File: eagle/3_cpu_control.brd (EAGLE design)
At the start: 160 x 100 mm, 50 parts, among them IC1 74LS151N, IC10 74LS173N, IC11 74LS74N, IC12 74LS74N, IC13 74LS541N, IC14 74LS541N, IC15 74LS21N, IC16 74LS02N, IC17 74LS02N, IC18 74LS04N, IC2 74LS151N, IC20 74LS08N, IC3 74LS153N, IC4 74LS153N, IC5 74LS541N, IC6 74LS32N, IC7 74LS08N, IC8 74LS151N, IC9 74LS157N

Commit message: Renamed F6 to /FP
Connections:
- net F6 renamed /FP
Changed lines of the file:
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@@
 <wire x1="48.26" y1="57.4675" x2="48.26" y2="58.7375" width="0.4064" layer="1"/>
 </signal>
-<signal name="F6">
+<signal name="/FP">
 <contactref element="IC11" pad="9"/>
 <contactref element="IC5" pad="8"/>

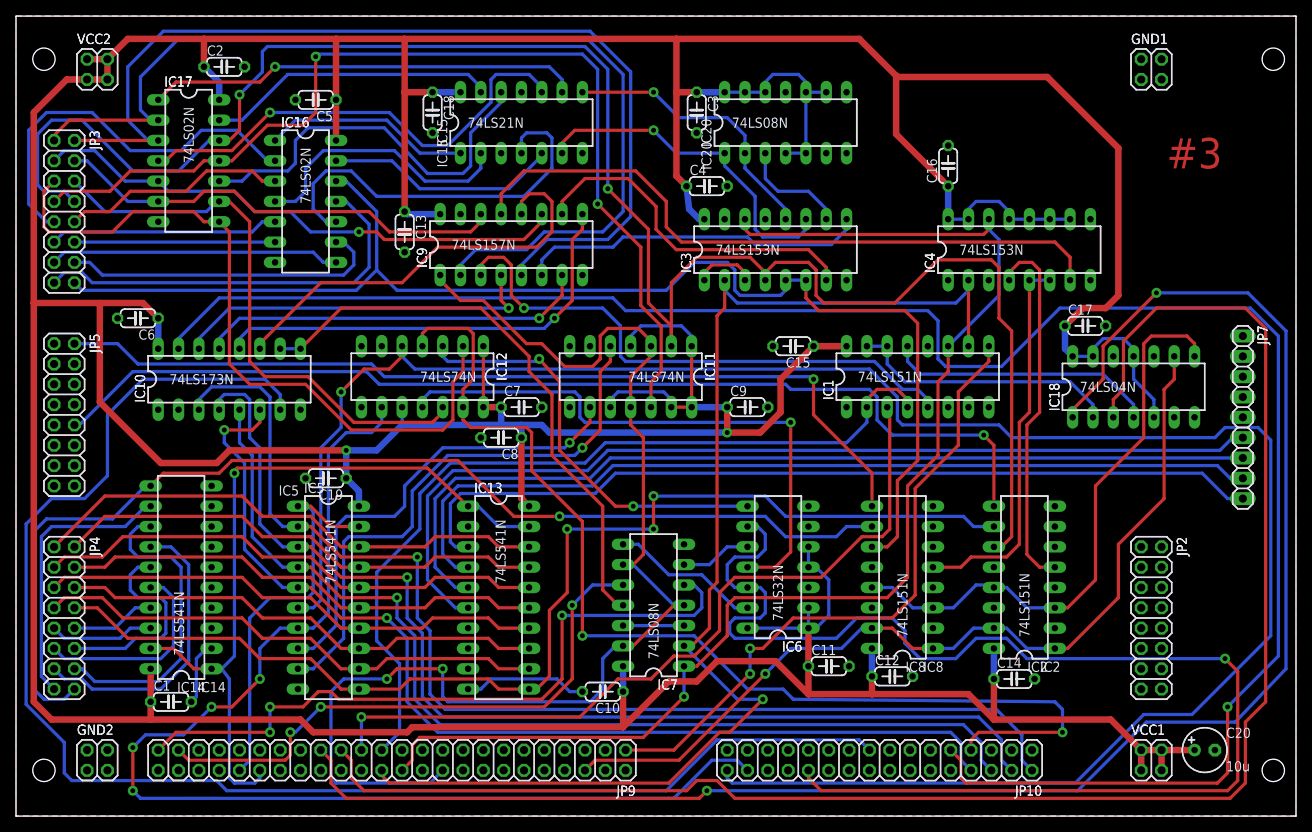
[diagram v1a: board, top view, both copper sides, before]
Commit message: Added /FP (flag paging enabled) to schematics and board, extended header connector
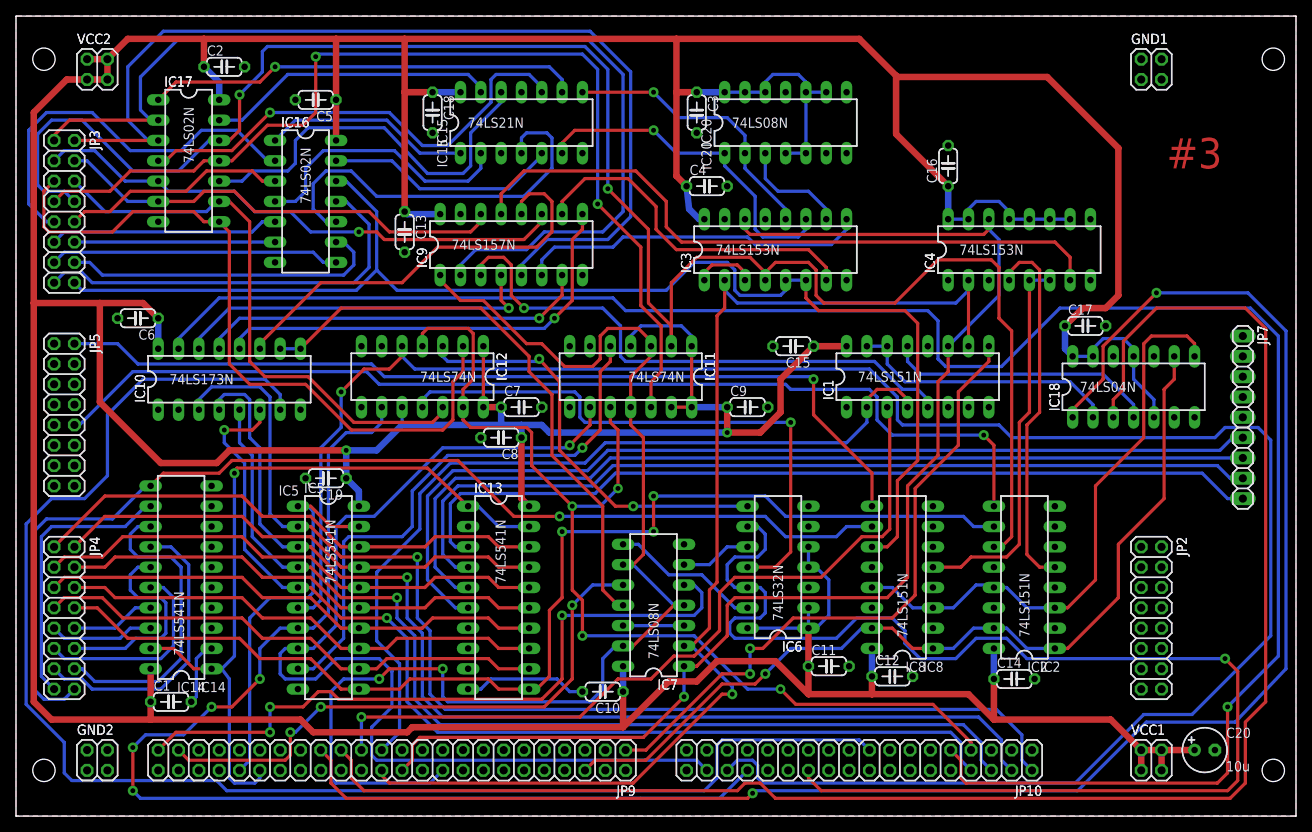
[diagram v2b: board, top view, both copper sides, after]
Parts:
- JP10: device pinhead:2X16 -> pinhead:2X18
- moved JP10 2.54 mm to (105.4, 6.99)
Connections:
- net +5V: no longer IC11.10
- net /FP: now also JP10.34
- net /RST: now also IC11.10
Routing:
- net /FP: track 58.9 -> 132.8 mm
- net +5V: track 853.1 -> 842.8 mm
- net /RST: track 136.7 -> 129.3 mm, vias 2 -> 4
- net LOAD_FLAGS1: track 156.6 -> 149.5 mm
- net CLK0D: track 184.2 -> 186.6 mm
- net /FI: track 259.2 -> 260.7 mm
- net /FS: track 149.1 -> 148.1 mm

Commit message: All boards prepared for MMU extension
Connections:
- new net /IO: JP10.35
- new net /NP_FAULT: JP10.36
- new net /WR_FAULT: JP10.33
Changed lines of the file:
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@@
 <contactref element="JP5" pad="4"/>
+</signal>
+<signal name="/WR_FAULT">
+<contactref element="JP10" pad="33"/>
+</signal>
+<signal name="/NP_FAULT">
+<contactref element="JP10" pad="36"/>
+</signal>
+<signal name="/IO">
+<contactref element="JP10" pad="35"/>
 </signal>
 </signals>

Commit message: Removal of PPC started
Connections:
- removed net /LDPPC: JP10.11
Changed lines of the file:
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@@
 <contactref element="JP10" pad="1"/>
-</signal>
-<signal name="/LDPPC">
-<contactref element="JP10" pad="11"/>
 </signal>
 <signal name="BUSCLKA">

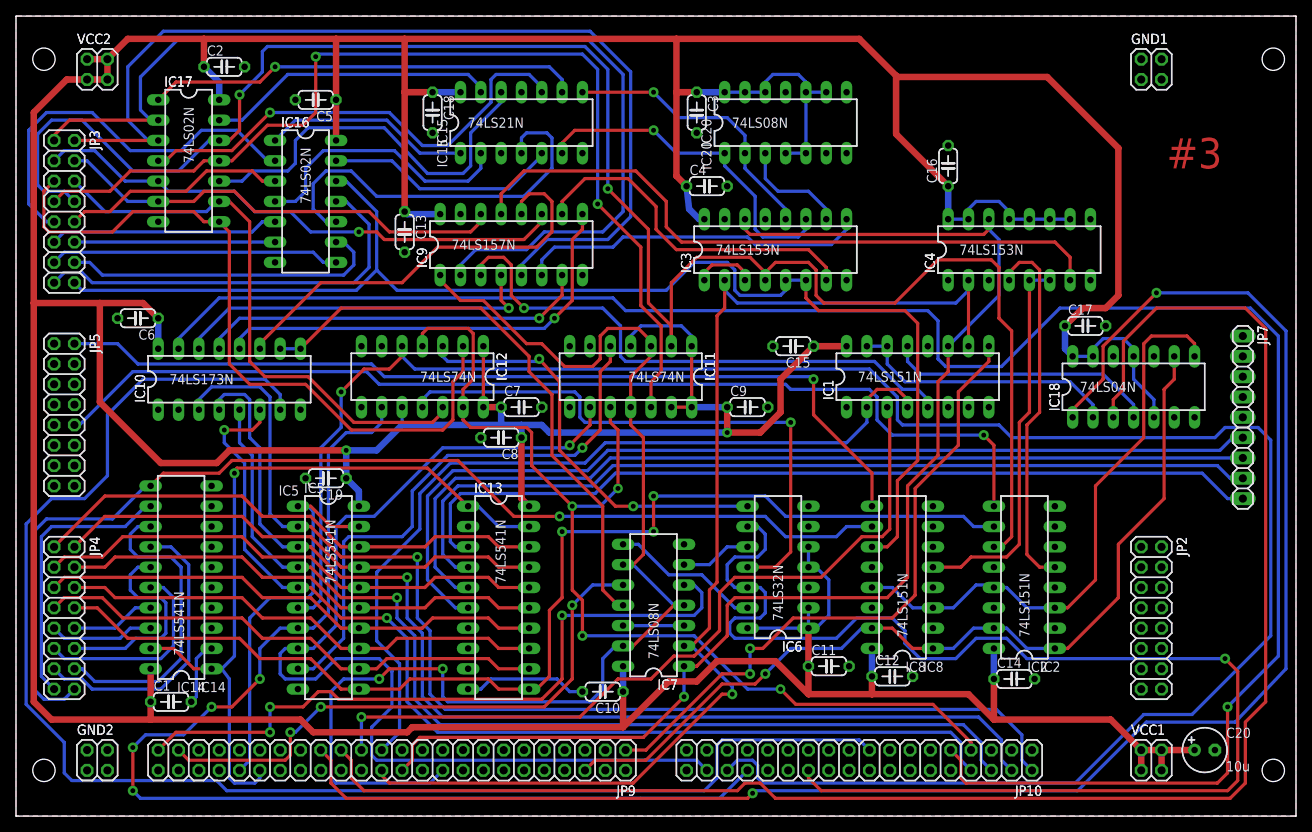
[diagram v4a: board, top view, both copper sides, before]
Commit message: Renumbered boards and schematic sheets
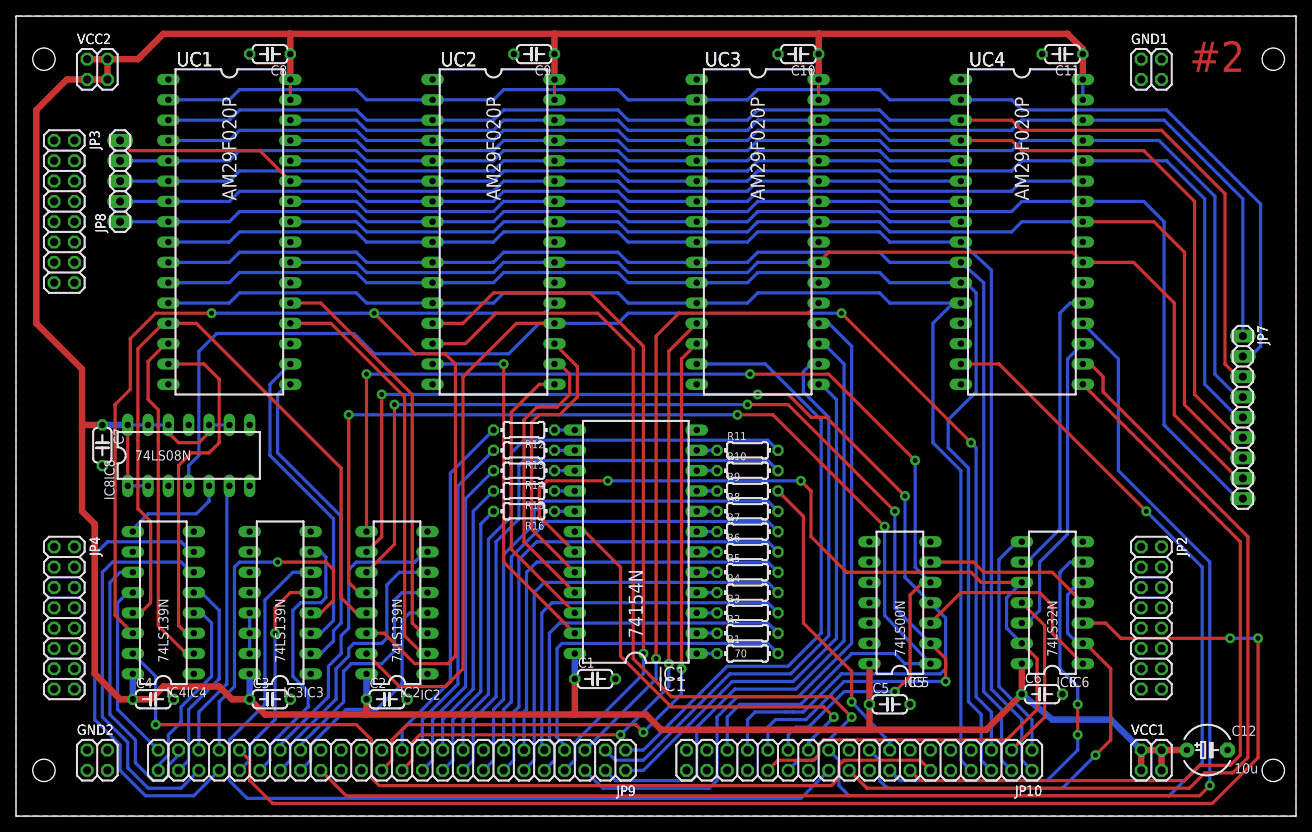
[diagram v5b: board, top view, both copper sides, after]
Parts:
- removed C13, C14, C15, C16, C17, C18, C19: 100n, rcl:C050-024X044
- removed C20: 10u, rcl:E2,5-6
- removed IC10: 74LS173N, 74xx-eu:DIL16
- removed IC11, IC12: 74LS74N, 74xx-eu:DIL14
- removed IC13, IC14: 74LS541N, 74xx-us:DIL20
- removed IC15: 74LS21N, 74xx-eu:DIL14
- removed IC16, IC17: 74LS02N, 74xx-eu:DIL14
- removed IC18: 74LS04N, 74xx-eu:DIL14
- removed IC20, IC7: 74LS08N, 74xx-eu:DIL14
- removed IC9: 74LS157N, 74xx-eu:DIL16
- removed JP5: (no value), pinhead:2X08
- added JP8: (no value), pinhead:1X05
- added R1: 70, rcl:0204/7
- added R10, R11, R12, R13, R14, R15, R16, R2, R3, R4, R5, R6, R7, R8, R9: (no value), rcl:0204/7
- added UC1, UC2, UC3, UC4: AM29F020P, am29-memory:DIL32-6
- C12: value 100n -> 10u; device rcl:C050-024X044 -> rcl:E5-6
- IC1: value 74LS151N -> 74154N; device 74xx-eu:DIL16 -> 74xx-eu:DIL24-6
- IC2: value 74LS151N -> 74LS139N
- IC3, IC4: value 74LS153N -> 74LS139N
- IC5: value 74LS541N -> 74LS00N; device 74xx-us:DIL20 -> 74xx-eu:DIL14
- IC8: value 74LS151N -> 74LS08N; device 74xx-eu:DIL16 -> 74xx-eu:DIL14
- moved C6 122.4 mm to (128.3, 15.2), turned to 0 degrees
- moved IC4 115.7 mm to (18.4, 26.7), turned to 90 degrees
- moved C5 104.2 mm to (109.2, 14.0), turned to 0 degrees
- moved C4 94.4 mm to (17.1, 14.6)
- moved C3 90.7 mm to (31.8, 14.6), turned to 0 degrees
- moved IC8 90.5 mm to (21.6, 45.1), turned to 0 degrees
- moved C10 83.4 mm to (97.8, 95.2)
- moved C11 81.9 mm to (130.8, 95.2), turned to 180 degrees
- moved C2 81.6 mm to (46.4, 14.6)
- moved IC2 78.5 mm to (47.6, 26.7)
- moved IC3 76.0 mm to (33.0, 26.7), turned to 90 degrees
- moved IC5 71.4 mm to (110.5, 26.7), turned to 90 degrees
- moved C8 56.0 mm to (31.8, 95.2)
- moved C1 53.1 mm to (72.4, 17.1)
- moved C7 52.6 mm to (10.8, 46.4), turned to 270 degrees
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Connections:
- removed net ALU_C: IC1.5, IC9.3
- removed net ALU_N: IC3.7, IC9.10
- removed net ALU_V: IC4.7, IC9.13
- removed net ALU_Z: IC3.9, IC9.6
- removed net F7: IC11.5, IC5.9
- removed net LBUS0: JP5.15
- removed net LBUS1: JP5.16
- removed net LBUS10: JP5.5
- removed net LBUS11: JP5.6
- removed net LBUS12: JP5.3
- removed net LBUS13: JP5.4
- removed net LBUS14: JP5.1
- removed net LBUS15: IC8.9, JP5.2
- removed net LBUS2: JP5.13
- removed net LBUS3: JP5.14
- removed net LBUS4: JP5.11
- removed net LBUS5: JP5.12
- removed net LBUS6: JP5.9
- removed net LBUS7: IC2.9, JP5.10
- removed net LBUS8: JP5.7
- removed net LBUS9: JP5.8
- removed net N$10: IC15.9, IC17.1
- removed net N$11: IC15.10, IC17.4
- removed net N$12: IC15.12, IC17.10
- removed net N$13: IC15.13, IC17.13
- removed net N$14: IC15.6, IC20.1, IC3.11
- removed net N$16: IC20.3, IC3.10
- removed net N$17: IC10.10, IC10.9, IC7.11
- removed net N$19: IC2.5, IC4.4
- removed net N$2: IC1.13, IC18.4
- removed net N$21: IC18.8, IC2.13, IC2.3, IC8.13, IC8.3
- removed net N$3: IC1.14, IC1.15, IC18.2
- removed net N$32: IC10.14, IC9.4
- removed net N$48: IC10.13, IC9.7
- removed net N$49: IC10.12, IC9.9
- removed net N$50: IC10.11, IC9.12
- removed net N$51: IC7.12, IC7.3
- removed net N$52: IC12.3, IC6.8
- removed net N$53: IC12.11, IC6.11
- removed net N$54: IC6.10, IC7.6
- removed net N$55: IC6.13, IC7.8
- removed net N$6: IC15.1, IC16.1
- removed net N$7: IC15.2, IC16.4
- removed net N$9: IC15.5, IC16.13
- new net /CNT_SP: IC6.12, UC4.19
- new net /INC_PC: IC6.9, UC4.21
- new net /LATCH_NONE: IC4.9, IC8.5
- new net ADDRBUS0: IC4.2, UC1.14
- new net ADDRBUS1: IC4.3, UC1.15
- new net BUSIFCMODE0: IC2.14, IC4.14, UC2.21
- new net BUSIFCMODE1: IC2.13, IC4.13, UC1.13
- new net CLBUS0: IC2.2, UC1.20
- new net CLBUS1: IC2.3, UC1.21
- new net CNT0: JP8.1, UC1.8, UC2.8, UC3.8, UC4.8
- new net CNT1: JP8.2, UC1.7, UC2.7, UC3.7, UC4.7
- new net CNT2: JP8.3, UC1.6, UC2.6, UC3.6, UC4.6
- new net CNT3: JP8.4, UC1.5, UC2.5, UC3.5, UC4.5
- new net CNT4: JP8.5, UC1.27, UC2.27, UC3.27, UC4.27
- new net CRBUS0: IC3.2, UC1.17
- new net CRBUS1: IC3.3, UC1.18
- new net LOAD0: IC1.23, UC2.15
- new net LOAD1: IC1.22, UC2.17
- new net LOAD2: IC1.21, UC2.18
- new net LOAD3: IC1.20, UC2.19
- new net N$31: IC1.1, R1.1
- new net N$33: IC1.2, R2.1
- new net N$34: IC1.3, R3.1
- new net N$35: IC1.4, R4.1
- new net N$36: IC1.5, R5.1
- new net N$37: IC1.6, R6.1
- new net N$38: IC1.7, R7.1
- new net N$39: IC1.8, R8.1
- new net N$40: IC1.9, R9.1
- new net N$41: IC1.10, R10.1
- new net N$42: IC1.11, R11.1
- new net N$43: IC1.13, R12.1
- new net N$44: IC1.14, R13.1
- new net N$45: IC1.15, R14.1
- new net N$56: IC1.17, R16.1
- net +5V: now also C12.+, IC1.24, IC5.14, IC8.1, IC8.10, IC8.12, IC8.13, IC8.14, IC8.2, IC8.9, UC1.31, UC1.32, UC2.31, UC2.32, UC3.31, UC3.32, UC4.31, UC4.32; no longer C12.1, C13.1, C14.1, C15.1, C16.1, C17.1, C18.1, C19.1, C20.+, IC1.16, IC10.16, IC11.1, IC11.13, IC11.14, IC11.4, IC12.1, IC12.10, IC12.14, IC13.20, IC14.20, IC15.14, IC16.14, IC17.14, IC18.11, IC18.13, IC18.14, IC18.5, IC20.10, IC20.12, IC20.13, IC20.14, IC20.4, IC20.5, IC20.9, IC4.10, IC4.11, IC4.12, IC4.13, IC4.15, IC5.20, IC6.1, IC6.2, IC6.4, IC6.5, IC7.14, IC8.16, IC9.16
- net /ALUCARRYIN: now also UC3.17
- net /ALUHI2MEM: now also IC2.9, IC5.5
- net /ALULO2MEM: now also IC2.10, IC5.4
- net /ALUSHR: now also UC3.15; no longer IC1.9
- net /BUSIFCEN: now also IC2.15, IC8.4, UC2.20
- net /CARRY1: no longer IC18.3
- net /CARRY3: no longer IC18.1
- net /CNTSP: now also IC6.11
- net /ENA: now also IC2.5
- net /ENABUS: now also IC3.6
- net /ENALU: now also IC6.3
- net /ENDP: now also IC4.6
- net /ENIPTR: now also IC3.7; no longer IC13.1, IC13.19, IC14.1, IC14.19
- net /ENLMDR: now also IC2.4
- net /ENMAR: now also IC4.4
- net /ENMEM: now also IC6.6
- net /ENMSW: now also IC3.5; no longer IC5.1, IC5.19
- net /ENPC: now also IC4.7
- net /ENRMDR: now also IC3.4
- net /ENSP: now also IC4.5
- net /ENX: now also IC2.6
- net /ENY: now also IC2.7
- net /FI: no longer IC12.5, IC5.6
- net /FP: no longer IC11.9, IC5.8
- net /FS: no longer IC12.9, IC5.7
- net /INCPC: now also IC6.8
- net /INC_MAR: now also UC4.20
- net /LATCHFLAGS: now also IC4.15
- net /LATCH_I: now also IC4.12; no longer IC7.5
- net /LATCH_S: now also IC4.11; no longer IC7.10
- net /LDA: now also R6.2
- net /LDAHI: now also R5.2
- net /LDALO: now also R4.2
- net /LDDP: now also R14.2
- net /LDMAR: now also R12.2
- net /LDMARHI: now also R11.2
- net /LDMARLO: now also R10.2
- net /LDMDR: now also R3.2
- net /LDMDRHI: now also R2.2
- net /LDMDRLO: now also R1.2
- net /LDMEM: now also R9.2
- net /LDMSW: now also R16.2; no longer IC11.11, IC11.3, IC7.13, IC7.4, IC7.9, IC9.1
- net /LDPC: now also R15.2
- net /LDSP: now also R13.2
- net /LDX: now also R7.2
- net /LDY: now also R8.2
- net /LOAD_IR: now also UC2.14
- net /MEM2ALUHI: now also IC2.11, IC5.2
- net /MEM2ALULO: now also IC2.12, IC5.1
- net /RST: no longer IC11.10, IC12.13, IC12.4
- net ALUBUS0: no longer IC17.2, IC9.2
- net ALUBUS1: no longer IC17.3, IC9.5
- net ALUBUS10: no longer IC16.5
- net ALUBUS11: no longer IC16.6
- net ALUBUS12: no longer IC16.8
- net ALUBUS13: no longer IC16.9
- net ALUBUS14: no longer IC16.11
- net ALUBUS15: no longer IC16.12, IC3.5, IC3.6, IC8.11
- net ALUBUS2: no longer IC17.5, IC9.11
- net ALUBUS3: no longer IC17.6, IC9.14
- net ALUBUS4: no longer IC12.2, IC17.8
- net ALUBUS5: no longer IC12.12, IC17.9
- net ALUBUS6: no longer IC11.12, IC17.11
- net ALUBUS7: no longer IC11.2, IC17.12, IC2.11, IC3.4
- net ALUBUS8: no longer IC16.2
- net ALUBUS9: no longer IC16.3
- net ALUMODE: now also UC3.18
- net ALUOP0: now also UC3.19
- net ALUOP1: now also UC3.20; no longer IC18.9, IC2.1, IC2.15, IC8.1, IC8.15
- net ALUOP2: now also UC3.21
- net ALUOP3: now also UC2.13
- net ALURES0: no longer IC1.2, IC1.4
- net ALURES8: no longer IC1.3
- net BUSCLKA: now also IC1.18
- net BUSCLKB: no longer IC6.12, IC6.9
- net CLK0D: now also IC6.2, IC6.5; no longer IC10.7
- net FAULT: now also IC1.19, IC6.10, IC6.13
- net FC: now also UC1.9, UC2.9, UC3.9, UC4.9; no longer IC10.3, IC5.2
- net FN: now also UC1.11, UC2.11, UC3.11, UC4.11; no longer IC10.5, IC5.4
- net FV: now also UC1.12, UC2.12, UC3.12, UC4.12; no longer IC10.6, IC5.5
- net FZ: now also UC1.10, UC2.10, UC3.10, UC4.10; no longer IC10.4, IC5.3
- net GND: now also C12.-, IC2.1, IC3.14, IC5.12, IC5.13, IC5.7, IC5.9, UC1.16, UC1.22, UC1.24, UC2.16, UC2.22, UC2.24, UC3.16, UC3.22, UC3.24, UC4.16, UC4.22, UC4.24; no longer C12.2, C13.2, C14.2, C15.2, C16.2, C17.2, C18.2, C19.2, C20.-, IC1.1, IC1.7, IC1.8, IC10.1, IC10.2, IC10.8, IC11.7, IC12.7, IC13.10, IC13.2, IC13.7, IC13.8, IC13.9, IC14.10, IC14.2, IC14.3, IC14.4, IC14.5, IC14.6, IC14.7, IC14.8, IC14.9, IC15.7, IC16.7, IC17.7, IC18.7, IC2.12, IC2.14, IC2.2, IC2.4, IC2.7, IC20.7, IC3.3, IC4.3, IC7.7, IC8.12, IC8.14, IC8.2, IC8.4, IC8.8, IC9.15, IC9.8
- net LOAD_FLAGS0: now also UC3.13; no longer IC1.11, IC3.14, IC4.14, IC7.1
- net LOAD_FLAGS1: now also UC3.14; no longer IC1.10, IC3.2, IC4.2, IC7.2
- net MDRLDINHBT: now also IC8.6
- net MEMSEG: now also UC4.17
- net N$1: now also IC1.16, R15.1; no longer IC4.5, IC4.6, IC8.5
- net N$15: now also IC5.6, IC6.4; no longer IC15.8, IC20.2, IC3.12
- net N$8: now also IC5.3, IC6.1; no longer IC15.4, IC16.10
- net OP0: now also UC1.26, UC2.26, UC3.26, UC4.26; no longer IC13.3
- net OP1: now also UC1.23, UC2.23, UC3.23, UC4.23; no longer IC13.4
- net OP2: now also UC1.25, UC2.25, UC3.25, UC4.25; no longer IC13.5
- net OP3: now also UC1.4, UC2.4, UC3.4, UC4.4; no longer IC13.6
- net OP4: now also UC1.28, UC2.28, UC3.28, UC4.28
- net OP5: now also UC1.29, UC2.29, UC3.29, UC4.29
- net OP6: now also UC1.3, UC2.3, UC3.3, UC4.3
- net OP7: now also UC1.2, UC2.2, UC3.2, UC4.2
- net OP8: now also UC1.30, UC2.30, UC3.30, UC4.30
- net PROT: now also UC4.15
- net RBUS0: no longer IC13.18, IC5.18
- net RBUS1: no longer IC13.17, IC5.17
- net RBUS10: no longer IC14.16
- net RBUS11: no longer IC14.15
- net RBUS12: no longer IC14.14
- net RBUS13: no longer IC14.13
- net RBUS14: no longer IC14.12
- net RBUS15: no longer IC14.11, IC8.10
- net RBUS2: no longer IC13.16, IC5.16
- net RBUS3: no longer IC13.15, IC5.15
- net RBUS4: no longer IC13.14, IC5.14
- net RBUS5: no longer IC13.13, IC5.13
- net RBUS6: no longer IC13.12, IC5.12
- net RBUS7: no longer IC13.11, IC2.10, IC5.11
- net RBUS8: no longer IC14.18
- net RBUS9: no longer IC14.17
- net RST: no longer IC10.15
- net SP_DIR: now also UC4.18
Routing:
- net +5V: track 842.8 -> 457.2 mm, vias 2 -> 0
- net /FI: track 260.7 -> 0.00 mm, vias 1 -> 0
- net RST: track 247.0 -> 0.00 mm, vias 1 -> 0
- net ALUBUS7: track 232.2 -> 0.00 mm, vias 2 -> 0
- net /BUSIFCEN: track 0.00 -> 229.5 mm, vias 0 -> 2
- net /CARRY3: track 211.9 -> 0.00 mm, vias 2 -> 0
- net /CARRY1: track 206.9 -> 0.00 mm
- net /INC_MAR: track 0.00 -> 177.3 mm, vias 0 -> 1
- net /ENALU: track 0.00 -> 171.6 mm, vias 0 -> 2
- net BUSCLKB: track 166.2 -> 0.00 mm, vias 1 -> 0
- net OP7: track 0.00 -> 165.6 mm
- net OP6: track 0.00 -> 163.2 mm
- net ALUBUS15: track 163.0 -> 0.00 mm
- net BUSIFCMODE0: track 0.00 -> 155.8 mm, vias 0 -> 2
- net /MEM2ALULO: track 0.00 -> 149.2 mm, vias 0 -> 3
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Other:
- board text added: "#2"
- board text added: "70"
- board text added: "74154N"
- board text added: "74LS00N"
- board text added: "74LS139N"
- board text added: "AM29F020P"
- board text added: "JP8"
- board text added: "UC1"
- board text added: "UC2"
- board text added: "UC3"
- board text added: "UC4"
- board text removed: "#3"
- board text removed: "74LS02N"
- board text removed: "74LS04N"
- board text removed: "74LS151N"
- board text removed: "74LS153N"
- board text removed: "74LS157N"
- board text removed: "74LS173N"
- board text removed: "74LS21N"
- board text removed: "74LS541N"
- board text removed: "74LS74N"
- board text removed: "IC10"
- board text removed: "IC11"
- board text removed: "IC12"
- board text removed: "IC13"
- board text removed: "IC14"
- board text removed: "IC15"
- board text removed: "IC16"
- board text removed: "IC17"
- board text removed: "IC18"
- board text removed: "IC20"
- board text removed: "IC7"
- board text removed: "IC9"
- board text removed: "JP5"

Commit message: Sat Feb  6 20:10:54 CET 2016
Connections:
- new net /IRET: UC4.13
- new net /MEMOP: UC4.14
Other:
- board text added: "#3"
- board text removed: "#2"
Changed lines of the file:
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@@
 <wire x1="160" y1="100" x2="0" y2="100" width="0" layer="20"/>
 <wire x1="0" y1="100" x2="0" y2="0" width="0" layer="20"/>
-<text x="146.685" y="93.0275" size="3.81" layer="1" font="vector" ratio="15">#2</text>
+<text x="146.685" y="93.0275" size="3.81" layer="1" font="vector" ratio="15">#3</text>
 <wire x1="-4.7625" y1="100.0125" x2="-4.7625" y2="109.5375" width="0.2032" layer="100"/>
 <wire x1="0" y1="104.775" x2="-9.525" y2="104.775" width="0.2032" layer="100"/>
@@
 <contactref element="JP10" pad="35"/>
 </signal>
+<signal name="/MEMOP">
+<contactref element="UC4" pad="14"/>
+</signal>
+<signal name="/IRET">
+<contactref element="UC4" pad="13"/>
+</signal>
 </signals>

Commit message: Mon Feb  8 16:27:58 CET 2016
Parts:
- JP8: device pinhead:1X05 -> pinhead:1X06
- moved JP8 1.27 mm to (13.0, 78.1)
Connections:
- removed net /IRET: UC4.13
- new net /FRET: JP8.1, UC1.19
- net /MEMOP: now also JP10.11
- net CNT0: now also JP8.2; no longer JP8.1
- net CNT1: now also JP8.3; no longer JP8.2
- net CNT2: now also JP8.4; no longer JP8.3
- net CNT3: now also JP8.5; no longer JP8.4
- net CNT4: now also JP8.6; no longer JP8.5
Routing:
- net /FRET: track 0.00 -> 26.5 mm
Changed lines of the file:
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@@
 <layer number="21" name="tPlace" color="7" fill="1" visible="no" active="yes"/>
 <layer number="22" name="bPlace" color="7" fill="1" visible="no" active="yes"/>
-<layer number="23" name="tOrigins" color="15" fill="1" visible="no" active="yes"/>
+<layer number="23" name="tOrigins" color="15" fill="1" visible="yes" active="yes"/>
 <layer number="24" name="bOrigins" color="15" fill="1" visible="no" active="yes"/>
 <layer number="25" name="tNames" color="7" fill="1" visible="no" active="yes"/>
@@
 <wire x1="13.6525" y1="83.185" x2="14.2875" y2="83.82" width="0.254" layer="121"/>
 <wire x1="14.2875" y1="85.09" x2="14.2875" y2="83.82" width="0.254" layer="121"/>
-<text x="11.1887" y="72.9488" size="1.27" layer="121" font="vector" ratio="20" rot="R90">JP8</text>
+<text x="11.1887" y="70.4088" size="1.27" layer="121" font="vector" ratio="20" rot="R90">JP8</text>
 <wire x1="77.47" y1="8.89" x2="76.835" y2="9.525" width="0.254" layer="121"/>
 <wire x1="76.835" y1="9.525" x2="75.565" y2="9.525" width="0.254" layer="121"/>
@@
 <wire x1="85.09" y1="5.08" x2="85.09" y2="8.89" width="0.254" layer="121"/>
 <wire x1="82.55" y1="5.08" x2="82.55" y2="8.89" width="0.254" layer="121"/>
+<wire x1="11.7475" y1="71.12" x2="11.7475" y2="72.39" width="0.254" layer="121"/>
+<wire x1="11.7475" y1="72.39" x2="12.3825" y2="73.025" width="0.254" layer="121"/>
+<wire x1="13.6525" y1="73.025" x2="14.2875" y2="72.39" width="0.254" layer="121"/>
+<wire x1="12.3825" y1="70.485" x2="13.6525" y2="70.485" width="0.254" layer="121"/>
+<wire x1="11.7475" y1="71.12" x2="12.3825" y2="70.485" width="0.254" layer="121"/>
+<wire x1="13.6525" y1="70.485" x2="14.2875" y2="71.12" width="0.254" layer="121"/>
+<wire x1="14.2875" y1="72.39" x2="14.2875" y2="71.12" width="0.254" layer="121"/>
 </plain>
 <attributes>
@@
 <element name="C11" library="rcl" package="C050-024X044" value="100n" x="130.81" y="95.25" rot="R180"/>
 <element name="C12" library="rcl" package="E5-6" value="10u" x="148.9075" y="8.255"/>
-<element name="JP8" library="pinhead" package="1X05" value="" x="13.0175" y="79.375" rot="R90"/>
+<element name="JP8" library="pinhead" package="1X06" value="" x="13.0175" y="78.105" rot="R90"/>
 <element name="JP7" library="pinhead" package="1X09" value="" x="153.3525" y="49.8475" rot="R270"/>
 <element name="IC3" library="74xx-eu" package="DIL16" value="74LS139N" x="33.02" y="26.67" rot="R90"/>
@@
 <wire x1="27.94" y1="75.565" x2="26.67" y2="74.295" width="0.4064" layer="16"/>
 <wire x1="26.67" y1="74.295" x2="19.05" y2="74.295" width="0.4064" layer="16"/>
-<contactref element="JP8" pad="1"/>
+<contactref element="JP8" pad="2"/>
 <wire x1="13.0175" y1="74.295" x2="19.05" y2="74.295" width="0.4064" layer="16"/>
 </signal>
@@
 <wire x1="27.94" y1="78.105" x2="26.67" y2="76.835" width="0.4064" layer="16"/>
 <wire x1="26.67" y1="76.835" x2="19.05" y2="76.835" width="0.4064" layer="16"/>
-<contactref element="JP8" pad="2"/>
+<contactref element="JP8" pad="3"/>
 <wire x1="13.0175" y1="76.835" x2="19.05" y2="76.835" width="0.4064" layer="16"/>
 </signal>
@@
 <wire x1="27.94" y1="80.645" x2="26.67" y2="79.375" width="0.4064" layer="16"/>
 <wire x1="26.67" y1="79.375" x2="19.05" y2="79.375" width="0.4064" layer="16"/>
-<contactref element="JP8" pad="3"/>
+<contactref element="JP8" pad="4"/>
 <wire x1="13.0175" y1="79.375" x2="19.05" y2="79.375" width="0.4064" layer="16"/>
 </signal>
@@
 <wire x1="27.94" y1="83.185" x2="26.67" y2="81.915" width="0.4064" layer="16"/>
 <wire x1="26.67" y1="81.915" x2="19.05" y2="81.915" width="0.4064" layer="16"/>
-<contactref element="JP8" pad="4"/>
+<contactref element="JP8" pad="5"/>
 <wire x1="13.0175" y1="81.915" x2="19.05" y2="81.915" width="0.4064" layer="16"/>
 </signal>
@@
 <wire x1="43.815" y1="78.105" x2="42.545" y2="79.375" width="0.4064" layer="16"/>
 <wire x1="42.545" y1="79.375" x2="34.29" y2="79.375" width="0.4064" layer="16"/>
-<contactref element="JP8" pad="5"/>
+<contactref element="JP8" pad="6"/>
 <wire x1="34.29" y1="79.375" x2="30.48" y2="83.185" width="0.4064" layer="1"/>
 <wire x1="30.48" y1="83.185" x2="14.2875" y2="83.185" width="0.4064" layer="1"/>
@@
 <signal name="/MEMOP">
 <contactref element="UC4" pad="14"/>
+<contactref element="JP10" pad="11"/>
+<wire x1="114.3" y1="8.255" x2="118.11" y2="59.055" width="0" layer="19" extent="1-1"/>
 </signal>
-<signal name="/IRET">
-<contactref element="UC4" pad="13"/>
+<signal name="/FRET">
+<contactref element="UC1" pad="19"/>
+<contactref element="JP8" pad="1"/>
+<wire x1="34.29" y1="59.055" x2="32.385" y2="59.055" width="0.4064" layer="1"/>
+<wire x1="32.385" y1="59.055" x2="20.955" y2="70.485" width="0.4064" layer="1"/>
+<wire x1="20.955" y1="70.485" x2="15.5575" y2="70.485" width="0.4064" layer="1"/>
+<wire x1="15.5575" y1="70.485" x2="14.2875" y2="71.755" width="0.4064" layer="1"/>
+<wire x1="14.2875" y1="71.755" x2="13.0175" y2="71.755" width="0.4064" layer="1"/>
 </signal>
 </signals>
